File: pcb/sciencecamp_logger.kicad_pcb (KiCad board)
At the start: 2 copper layers, 97 x 46 mm, 33 parts, among them J1 1-Wire, J2 HC-SR04, J3 OLED, J4 Micro_SD_Card_Det, SW1 OFF/ON, SW2 action, U1 74LVC125, U2 AMS1117-3.3

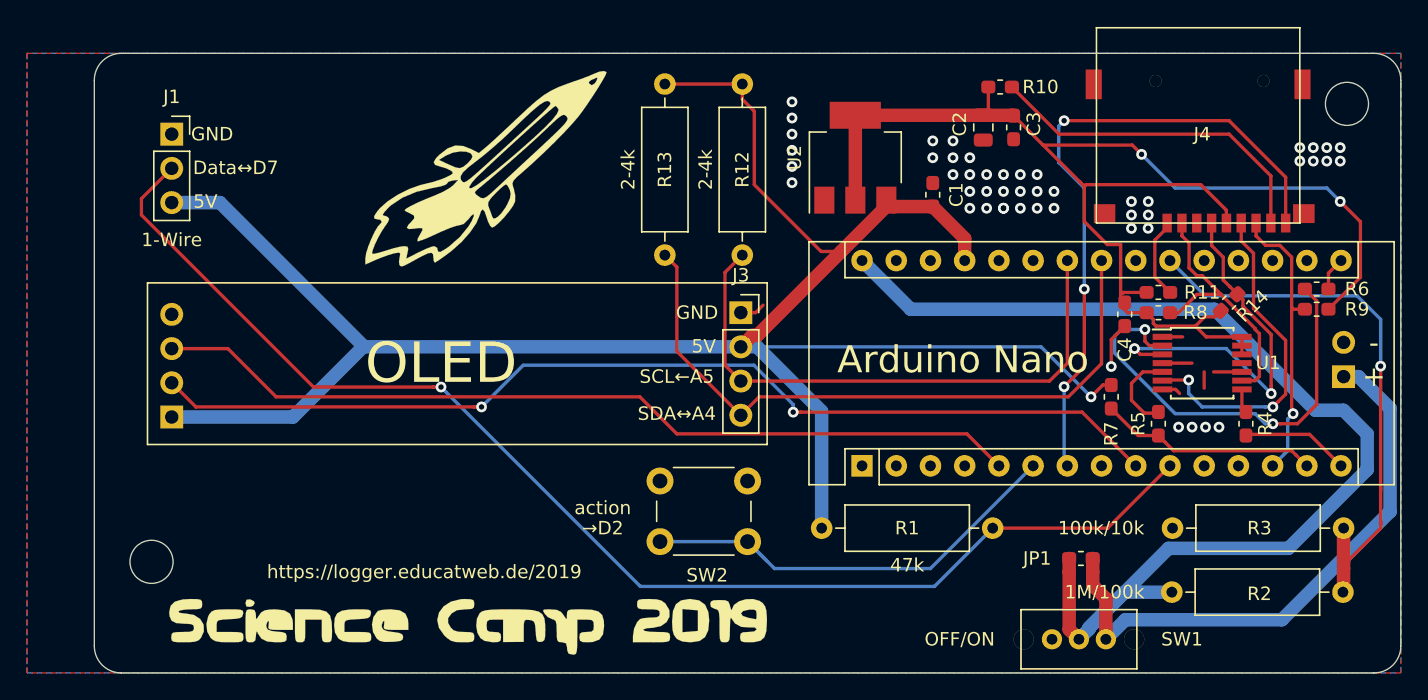
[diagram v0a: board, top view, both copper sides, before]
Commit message: FIX: server layout issues
- wrong pin order for sc-card slot
- wrong pin order for ultrasonic sensor
- wrong footprint for 10uF cap
- missing pads for switch  footprint
- missing level convertion for spi chip select
- unnecessary level conversion for miso
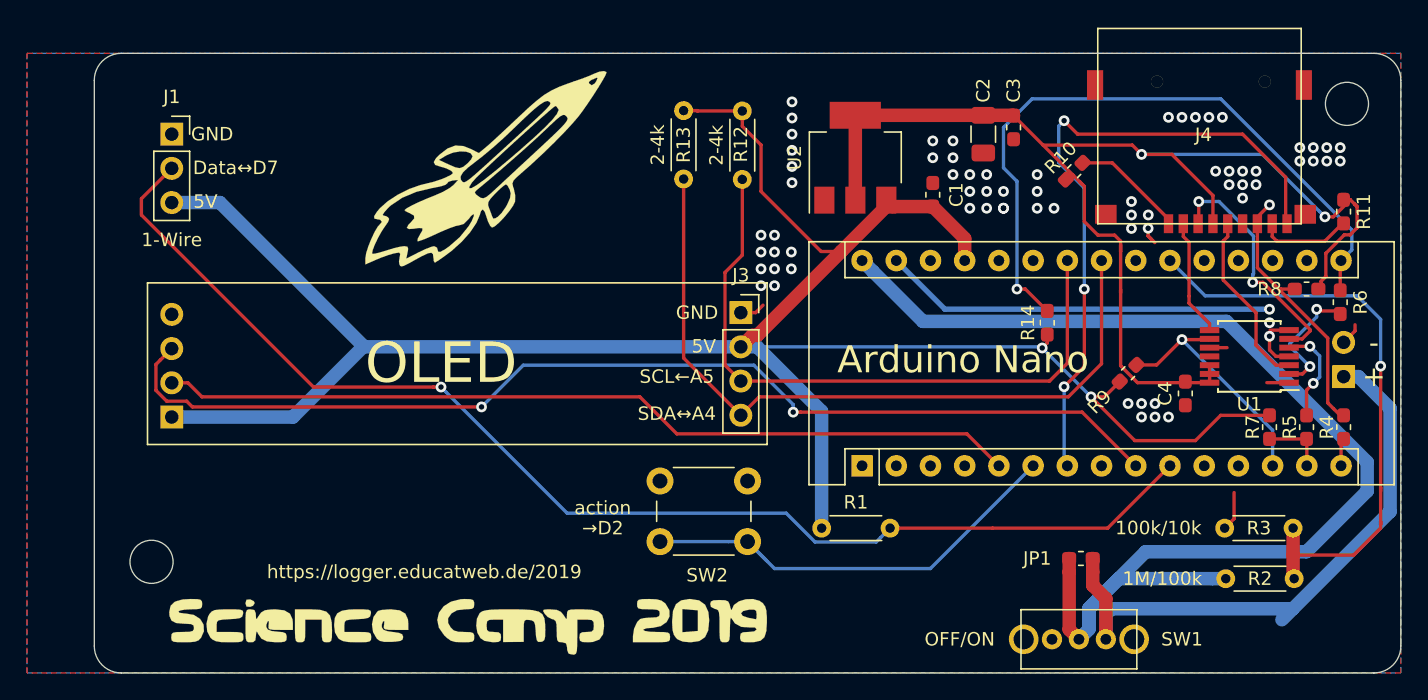
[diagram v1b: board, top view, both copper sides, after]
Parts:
- C2: footprint Capacitor_SMD:C_0805_2012Metric -> Capacitor_SMD:C_1206_3216Metric
- R1, R12, R13, R2, R3: footprint Resistor_THT:R_Axial_DIN0309_L9.0mm_D3.2mm_P12.70mm_Horizontal -> Resistor_THT:R_Axial_DIN0204_L3.6mm_D1.6mm_P5.08mm_Horizontal
- R4, R5, R6: value R -> 0
- moved R11 15.0 mm to (204.8, 87.8), turned to 270 degrees
- moved R9 14.8 mm to (188.8, 99.8), turned to 45 degrees
- moved R14 13.6 mm to (182.8, 96.0), turned to 90 degrees
- moved R7 12.0 mm to (199.2, 103.8)
- moved R8 11.1 mm to (202.0, 93.5), turned to 180 degrees
- moved R5 11.0 mm to (202.0, 103.8)
- moved R10 8.33 mm to (184.8, 84.8), turned to 45 degrees
- moved C4 7.40 mm to (193.0, 101.2)
- moved R4 7.25 mm to (204.8, 103.8)
- moved J4 4.65 mm to (194.2, 82.2), turned to 270 degrees
- moved R2 4.12 mm to (196.0, 115.0)
- moved R3 3.75 mm to (201.0, 111.2)
- moved U1 3.54 mm to (197.8, 98.5), turned to 180 degrees
- moved R13 2.41 mm to (155.8, 80.2)
- moved R6 2.00 mm to (204.5, 94.5), turned to 90 degrees
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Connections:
- J2 pad 2: Net-(A1-Pad9) -> Net-(A1-Pad5)
- J2 pad 3: Net-(A1-Pad5) -> Net-(A1-Pad9)
- J4 pad 2: SD_SS -> Net-(J4-Pad2)
- R14 pad 1: SD_3V3 -> +5V
- R14 pad 2: Net-(J4-Pad5) -> SPI_SCK
- R4 pad 1: Net-(R4-Pad1) -> Net-(J4-Pad7)
- R9 pad 1: SD_3V3 -> +5V
- U1 pad 8: Net-(R4-Pad1) -> Net-(J4-Pad2)
- U1 pad 9: Net-(J4-Pad7) -> SD_SS
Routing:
- net SPI_SCK: track 2.53 -> 50.8 mm, vias 0 -> 1
- net GND: track 13.7 -> 44.3 mm, vias 49 -> 69
- net Net-(R6-Pad1): track 33.1 -> 9.28 mm
- net Net-(J4-Pad1): track 25.5 -> 8.81 mm
- net Net-(J4-Pad5): track 28.3 -> 13.2 mm, vias 2 -> 0
- net +5V: track 155.5 -> 169.6 mm, vias 1 -> 2
- net MOSI: track 16.3 -> 4.51 mm
- net Net-(J4-Pad2): track 0.00 -> 8.71 mm
- net Net-(J4-Pad3): track 25.0 -> 17.9 mm
- net MISO: track 8.03 -> 2.02 mm
- net /SCL: track 42.8 -> 48.4 mm
- net SD_3V3: track 100.2 -> 95.1 mm
- net /SDA: track 50.2 -> 55.3 mm
- net Net-(A1-Pad9): track 77.0 -> 81.6 mm
- net Net-(A1-Pad30): track 85.7 -> 90.1 mm
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
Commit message: Slight fixes
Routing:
- net SPI_SCK: track 50.8 -> 53.2 mm
- net SD_3V3: track 95.1 -> 94.4 mm
- net GND: vias 69 -> 72
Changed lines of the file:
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@@
     (thickness 1.6)
     (drawings 29)
-    (tracks 391)
+    (tracks 399)
     (zones 0)
     (modules 33)
@@
       (effects (font (size 1 1) (thickness 0.15)))
     )
-    (fp_text value Micro_SD_Card_Det (at 0 -5.2 270) (layer F.Fab)
-      (effects (font (size 1 1) (thickness 0.15)))
-    )
+    (fp_text value Micro_SD_Card_Det (at 0 -5.2 90) (layer F.Fab)
+      (effects (font (size 1 1) (thickness 0.15)))
+    )
+    (fp_line (start 6.4 -7.35) (end 6.4 7.75) (layer F.SilkS) (width 0.12))
+    (fp_line (start 6.4 7.75) (end -8.1 7.75) (layer F.SilkS) (width 0.12))
+    (fp_line (start -8.1 7.75) (end -8.1 -7.35) (layer F.SilkS) (width 0.12))
     (fp_line (start -8.1 -7.35) (end 6.4 -7.35) (layer F.SilkS) (width 0.12))
-    (fp_line (start -8.1 7.75) (end -8.1 -7.35) (layer F.SilkS) (width 0.12))
-    (fp_line (start 6.4 7.75) (end -8.1 7.75) (layer F.SilkS) (width 0.12))
-    (fp_line (start 6.4 -7.35) (end 6.4 7.75) (layer F.SilkS) (width 0.12))
+    (pad 11 smd rect (at -3.9 -7.55 180) (size 1.2 2.2) (layers F.Cu F.Paste F.Mask)
+      (net 2 GND))
+    (pad 11 smd rect (at -3.9 7.95 180) (size 1.2 2.2) (layers F.Cu F.Paste F.Mask)
+      (net 2 GND))
+    (pad 11 smd rect (at 5.7 -7.65 180) (size 1.6 1.4) (layers F.Cu F.Paste F.Mask)
+      (net 2 GND))
+    (pad 11 smd rect (at 5.7 7.15 180) (size 1.6 1.4) (layers F.Cu F.Paste F.Mask)
+      (net 2 GND))
+    (pad 10 smd rect (at 6.4 -6.3 180) (size 0.7 1.4) (layers F.Cu F.Paste F.Mask)
+      (net 39 SD_DETECT))
+    (pad 8 smd rect (at 6.4 -5.2 180) (size 0.7 1.4) (layers F.Cu F.Paste F.Mask)
+      (net 37 "Net-(J4-Pad8)"))
+    (pad 7 smd rect (at 6.4 -4.1 180) (size 0.7 1.4) (layers F.Cu F.Paste F.Mask)
+      (net 30 "Net-(J4-Pad7)"))
+    (pad 6 smd rect (at 6.4 -3 180) (size 0.7 1.4) (layers F.Cu F.Paste F.Mask)
+      (net 2 GND))
+    (pad 5 smd rect (at 6.4 -1.9 180) (size 0.7 1.4) (layers F.Cu F.Paste F.Mask)
+      (net 32 "Net-(J4-Pad5)"))
+    (pad 4 smd rect (at 6.4 -0.8 180) (size 0.7 1.4) (layers F.Cu F.Paste F.Mask)
+      (net 29 SD_3V3))
+    (pad 3 smd rect (at 6.4 0.3 180) (size 0.7 1.4) (layers F.Cu F.Paste F.Mask)
+      (net 31 "Net-(J4-Pad3)"))
+    (pad 2 smd rect (at 6.4 1.4 180) (size 0.7 1.4) (layers F.Cu F.Paste F.Mask)
+      (net 41 "Net-(J4-Pad2)"))
+    (pad "" thru_hole circle (at -4.15 -4.65 180) (size 0.9 0.9) (drill 0.9) (layers *.Cu *.Mask))
+    (pad "" thru_hole circle (at -4.15 3.35 180) (size 0.9 0.9) (drill 0.9) (layers *.Cu *.Mask))
     (pad 1 smd rect (at 6.4 2.5 180) (size 0.7 1.4) (layers F.Cu F.Paste F.Mask)
       (net 36 "Net-(J4-Pad1)"))
-    (pad "" thru_hole circle (at -4.15 3.35 180) (size 0.9 0.9) (drill 0.9) (layers *.Cu *.Mask))
-    (pad "" thru_hole circle (at -4.15 -4.65 180) (size 0.9 0.9) (drill 0.9) (layers *.Cu *.Mask))
-    (pad 2 smd rect (at 6.4 1.4 180) (size 0.7 1.4) (layers F.Cu F.Paste F.Mask)
-      (net 41 "Net-(J4-Pad2)"))
-    (pad 3 smd rect (at 6.4 0.3 180) (size 0.7 1.4) (layers F.Cu F.Paste F.Mask)
-      (net 31 "Net-(J4-Pad3)"))
-    (pad 4 smd rect (at 6.4 -0.8 180) (size 0.7 1.4) (layers F.Cu F.Paste F.Mask)
-      (net 29 SD_3V3))
-    (pad 5 smd rect (at 6.4 -1.9 180) (size 0.7 1.4) (layers F.Cu F.Paste F.Mask)
-      (net 32 "Net-(J4-Pad5)"))
-    (pad 6 smd rect (at 6.4 -3 180) (size 0.7 1.4) (layers F.Cu F.Paste F.Mask)
-      (net 2 GND))
-    (pad 7 smd rect (at 6.4 -4.1 180) (size 0.7 1.4) (layers F.Cu F.Paste F.Mask)
-      (net 30 "Net-(J4-Pad7)"))
-    (pad 8 smd rect (at 6.4 -5.2 180) (size 0.7 1.4) (layers F.Cu F.Paste F.Mask)
-      (net 37 "Net-(J4-Pad8)"))
-    (pad 10 smd rect (at 6.4 -6.3 180) (size 0.7 1.4) (layers F.Cu F.Paste F.Mask)
-      (net 39 SD_DETECT))
-    (pad 11 smd rect (at 5.7 7.15 180) (size 1.6 1.4) (layers F.Cu F.Paste F.Mask)
-      (net 2 GND))
-    (pad 11 smd rect (at 5.7 -7.65 180) (size 1.6 1.4) (layers F.Cu F.Paste F.Mask)
-      (net 2 GND))
-    (pad 11 smd rect (at -3.9 7.95 180) (size 1.2 2.2) (layers F.Cu F.Paste F.Mask)
-      (net 2 GND))
-    (pad 11 smd rect (at -3.9 -7.55 180) (size 1.2 2.2) (layers F.Cu F.Paste F.Mask)
-      (net 2 GND))
   )
   (module Package_SO:TSSOP-14_4.4x5mm_P0.65mm (layer F.Cu)
@@
   (via (at 204.5 84) (size 0.8) (drill 0.4) (layers F.Cu B.Cu) (net 2))
   (via (at 203.5 84) (size 0.8) (drill 0.4) (layers F.Cu B.Cu) (net 2))
-  (via (at 202.5 84) (size 0.8) (drill 0.4) (layers F.Cu B.Cu) (net 2))
-  (via (at 201.5 84) (size 0.8) (drill 0.4) (layers F.Cu B.Cu) (net 2))
-  (via (at 201.5 83) (size 0.8) (drill 0.4) (layers F.Cu B.Cu) (net 2))
   (via (at 202.5 83) (size 0.8) (drill 0.4) (layers F.Cu B.Cu) (net 2))
   (via (at 203.5 83) (size 0.8) (drill 0.4) (layers F.Cu B.Cu) (net 2))
@@
   (segment (start 194.8 97.85) (end 196.1 97.85) (width 0.25) (layer F.Cu) (net 2))
   (via (at 190.75 102) (size 0.8) (drill 0.4) (layers F.Cu B.Cu) (net 2))
-  (via (at 195.75 80.75) (size 0.8) (drill 0.4) (layers F.Cu B.Cu) (net 2))
-  (via (at 194.75 80.75) (size 0.8) (drill 0.4) (layers F.Cu B.Cu) (net 2))
-  (via (at 193.75 80.75) (size 0.8) (drill 0.4) (layers F.Cu B.Cu) (net 2))
-  (via (at 192.75 80.75) (size 0.8) (drill 0.4) (layers F.Cu B.Cu) (net 2))
-  (via (at 191.75 80.75) (size 0.8) (drill 0.4) (layers F.Cu B.Cu) (net 2))
+  (via (at 195.25 80.5) (size 0.8) (drill 0.4) (layers F.Cu B.Cu) (net 2))
+  (via (at 194.25 80.5) (size 0.8) (drill 0.4) (layers F.Cu B.Cu) (net 2))
+  (via (at 193.25 80.5) (size 0.8) (drill 0.4) (layers F.Cu B.Cu) (net 2))
+  (via (at 192.25 80.5) (size 0.8) (drill 0.4) (layers F.Cu B.Cu) (net 2))
   (via (at 198.25 84.75) (size 0.8) (drill 0.4) (layers F.Cu B.Cu) (net 2))
   (via (at 197.25 84.75) (size 0.8) (drill 0.4) (layers F.Cu B.Cu) (net 2))
@@
   (via (at 161.5 92) (size 0.8) (drill 0.4) (layers F.Cu B.Cu) (net 2))
   (via (at 161.5 93.25) (size 0.8) (drill 0.4) (layers F.Cu B.Cu) (net 2))
+  (via (at 202.5 82) (size 0.8) (drill 0.4) (layers F.Cu B.Cu) (net 2))
+  (via (at 201.5 82) (size 0.8) (drill 0.4) (layers F.Cu B.Cu) (net 2))
+  (via (at 191.25 80.5) (size 0.8) (drill 0.4) (layers F.Cu B.Cu) (net 2))
+  (via (at 190.25 80.5) (size 0.8) (drill 0.4) (layers F.Cu B.Cu) (net 2))
+  (via (at 189.25 80.5) (size 0.8) (drill 0.4) (layers F.Cu B.Cu) (net 2))
+  (via (at 188.25 80.5) (size 0.8) (drill 0.4) (layers F.Cu B.Cu) (net 2))
+  (via (at 187.25 80.5) (size 0.8) (drill 0.4) (layers F.Cu B.Cu) (net 2))
   (segment (start 160 97.79) (end 131.96 97.79) (width 1) (layer B.Cu) (net 5))
   (segment (start 126.75 103) (end 117.75 103) (width 1) (layer B.Cu) (net 5))
@@
   (segment (start 179.5 84.5) (end 179.5 81.5) (width 0.25) (layer B.Cu) (net 26))
   (segment (start 179.5 84.5) (end 180.5 85.5) (width 0.25) (layer B.Cu) (net 26))
-  (segment (start 179.5 81.5) (end 181.625 79.375) (width 0.25) (layer B.Cu) (net 26))
-  (segment (start 181.625 79.375) (end 195.625 79.375) (width 0.25) (layer B.Cu) (net 26))
-  (segment (start 205.359999 89.109999) (end 195.625 79.375) (width 0.25) (layer B.Cu) (net 26))
+  (segment (start 181.25 79.75) (end 179.5 81.5) (width 0.25) (layer B.Cu) (net 26))
+  (segment (start 185 79.75) (end 181.25 79.75) (width 0.25) (layer B.Cu) (net 26))
+  (segment (start 185.25 79.5) (end 185 79.75) (width 0.25) (layer B.Cu) (net 26))
+  (segment (start 204.5 87.25) (end 196.75 79.5) (width 0.25) (layer B.Cu) (net 26))
+  (segment (start 196.75 79.5) (end 185.25 79.5) (width 0.25) (layer B.Cu) (net 26))
+  (segment (start 204.56 91.385) (end 204.56 90.25363) (width 0.25) (layer B.Cu) (net 26))
+  (segment (start 204.5 90.19363) (end 204.5 87.25) (width 0.25) (layer B.Cu) (net 26))
+  (segment (start 204.56 90.25363) (end 204.5 90.19363) (width 0.25) (layer B.Cu) (net 26))
   (segment (start 204.56 104.685) (end 204.5 104.625) (width 0.25) (layer F.Cu) (net 27))
   (segment (start 204.56 106.625) (end 204.56 104.685) (width 0.25) (layer F.Cu) (net 27))
@@
   (segment (start 187.75 89.5) (end 186.514998 89.5) (width 0.25) (layer F.Cu) (net 29))
   (segment (start 198.72468 83.5) (end 202.962341 87.737661) (width 0.25) (layer B.Cu) (net 29))
-  (via (at 203.36234 88.13766) (size 0.8) (drill 0.4) (layers F.Cu B.Cu) (net 29))
+  (via (at 203.5 88) (size 0.8) (drill 0.4) (layers F.Cu B.Cu) (net 29))
   (segment (start 202.962341 87.737661) (end 203.36234 88.13766) (width 0.25) (layer B.Cu) (net 29))
   (segment (start 189.75 83.5) (end 198.72468 83.5) (width 0.25) (layer B.Cu) (net 29))
-  (segment (start 203.98734 88.13766) (end 205.25 86.875) (width 0.25) (layer F.Cu) (net 29))
-  (segment (start 203.36234 88.13766) (end 203.98734 88.13766) (width 0.25) (layer F.Cu) (net 29))
   (segment (start 203.434999 90.844999) (end 204.804988 89.47501) (width 0.25) (layer F.Cu) (net 29))
   (segment (start 203.434999 92.565001) (end 203.434999 90.844999) (width 0.25) (layer F.Cu) (net 29))
@@
   (segment (start 205.75 88.95002) (end 205.75 87.375) (width 0.25) (layer F.Cu) (net 29))
   (segment (start 205.5625 87.1875) (end 205.25 86.875) (width 0.25) (layer F.Cu) (net 29))
+  (segment (start 204.625 86.875) (end 203.5 88) (width 0.25) (layer F.Cu) (net 29))
+  (segment (start 204.75 86.875) (end 204.625 86.875) (width 0.25) (layer F.Cu) (net 29))
   (via (at 199.25 87.25) (size 0.8) (drill 0.4) (layers F.Cu B.Cu) (net 30))
   (segment (start 198.35 88.65) (end 198.35 88.15) (width 0.25) (layer F.Cu) (net 30))
